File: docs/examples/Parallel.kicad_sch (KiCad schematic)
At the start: 2 parts

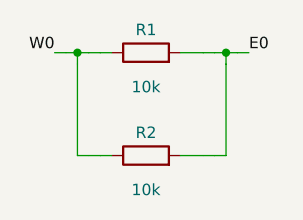
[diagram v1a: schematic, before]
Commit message: ERC-clean KiCad export: project + sym-lib-table, test points on open ports, automatic PWR_FLAGs from geometry nets; ERC (errors+warnings) asserted in tests
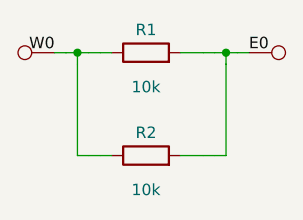
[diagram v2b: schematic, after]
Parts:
- added TP1, TP2: TestPoint, symbol Connector:TestPoint
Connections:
- net E0: now also TP1.1
- net W0: now also TP2.1
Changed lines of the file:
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@@
 		(instances
 			(project "Parallel"
-				(path "/a18f1573-c029-4e74-8901-a6d9135d9307"
+				(path "/4f701680-1782-4c66-b975-ed4bf6add8cb"
 					(reference "R1")
 					(unit 1)
@@
 		(instances
 			(project "Parallel"
-				(path "/a18f1573-c029-4e74-8901-a6d9135d9307"
+				(path "/4f701680-1782-4c66-b975-ed4bf6add8cb"
 					(reference "R2")
 					(unit 1)
 				)
+			)
+		)
+	)
+	(symbol
+		(lib_id "Connector:TestPoint")
+		(at 46.99 29.21 270)
+		(unit 1)
+		(exclude_from_sim yes)
+		(in_bom no)
+		(on_board yes)
+		(dnp no)
+		(property "Reference" "TP1"
+			(at 46.99 29.21 90)
+			(effects
+				(font
+					(size 1.27 1.27)
+				)
+				(hide yes)
+			)
+		)
+		(property "Value" "TestPoint"
+			(at 46.99 29.21 90)
+			(effects
+				(font
+					(size 1.27 1.27)
+				)
+				(hide yes)
+			)
+		)
+		(property "Footprint" ""
+			(at 46.99 29.21 90)
+			(effects
+				(font
+					(size 1.27 1.27)
+				)
+				(hide yes)
+			)
+		)
+		(property "Datasheet" ""
+			(at 46.99 29.21 90)
+			(effects
+				(font
+					(size 1.27 1.27)
+				)
+				(hide yes)
+			)
+		)
+		(pin "1"
+		)
+		(instances
+			(project "Parallel"
+				(path "/4f701680-1782-4c66-b975-ed4bf6add8cb"
+					(reference "TP1")
+					(unit 1)
+				)
+			)
+		)
+	)
+	(symbol
+		(lib_id "Connector:TestPoint")
+		(at 25.4 29.21 90)
+		(unit 1)
+		(exclude_from_sim yes)
+		(in_bom no)
+		(on_board yes)
+		(dnp no)
+		(property "Reference" "TP2"
+			(at 25.4 29.21 90)
+			(effects
+				(font
+					(size 1.27 1.27)
+				)
+				(hide yes)
+			)
+		)
+		(property "Value" "TestPoint"
+			(at 25.4 29.21 90)
+			(effects
+				(font
+					(size 1.27 1.27)
+				)
+				(hide yes)
+			)
+		)
+		(property "Footprint" ""
+			(at 25.4 29.21 90)
+			(effects
+				(font
+					(size 1.27 1.27)
+				)
+				(hide yes)
+			)
+		)
+		(property "Datasheet" ""
+			(at 25.4 29.21 90)
+			(effects
+				(font
+					(size 1.27 1.27)
+				)
+				(hide yes)
+			)
+		)
+		(pin "1"
+		)
+		(instances
+			(project "Parallel"
+				(path "/4f701680-1782-4c66-b975-ed4bf6add8cb"
+					(reference "TP2")
+					(unit 1)
+				)
